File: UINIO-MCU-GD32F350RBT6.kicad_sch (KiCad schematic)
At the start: 33 parts, among them J1 Conn_01x32_Pin, J2 Conn_01x32_Pin, J3 Conn_01x04_Pin, SW1 BOOT0, SW2 NRST, U1 ME6211C33M5G-N, U2 GD32F350RBT6, Y1 32.768KHz, Y2 8MHz

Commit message: Release UINIO-MCU-GD32F350RBT6 version 3.2.0.
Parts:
- removed R4: 1M, Resistor_SMD:R_0603_1608Metric, symbol Device:R
- removed R9: 1.5K, Resistor_SMD:R_0603_1608Metric, symbol Device:R
- added C11: 0.1uF, Capacitor_SMD:C_0603_1608Metric, symbol Device:C
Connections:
- net GND: now also U2.12 (VSSA), C11.2; no longer L1.1
- net VBAT: now also C11.1
- net VDD_3.3V: now also L1.1; no longer U2.13 (VDDA)
- net VSSA: no longer names the net of L1.2
- net VSSA: now also U2.13 (VDDA); no longer U2.12 (VSSA)
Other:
- moved on the sheet: L1

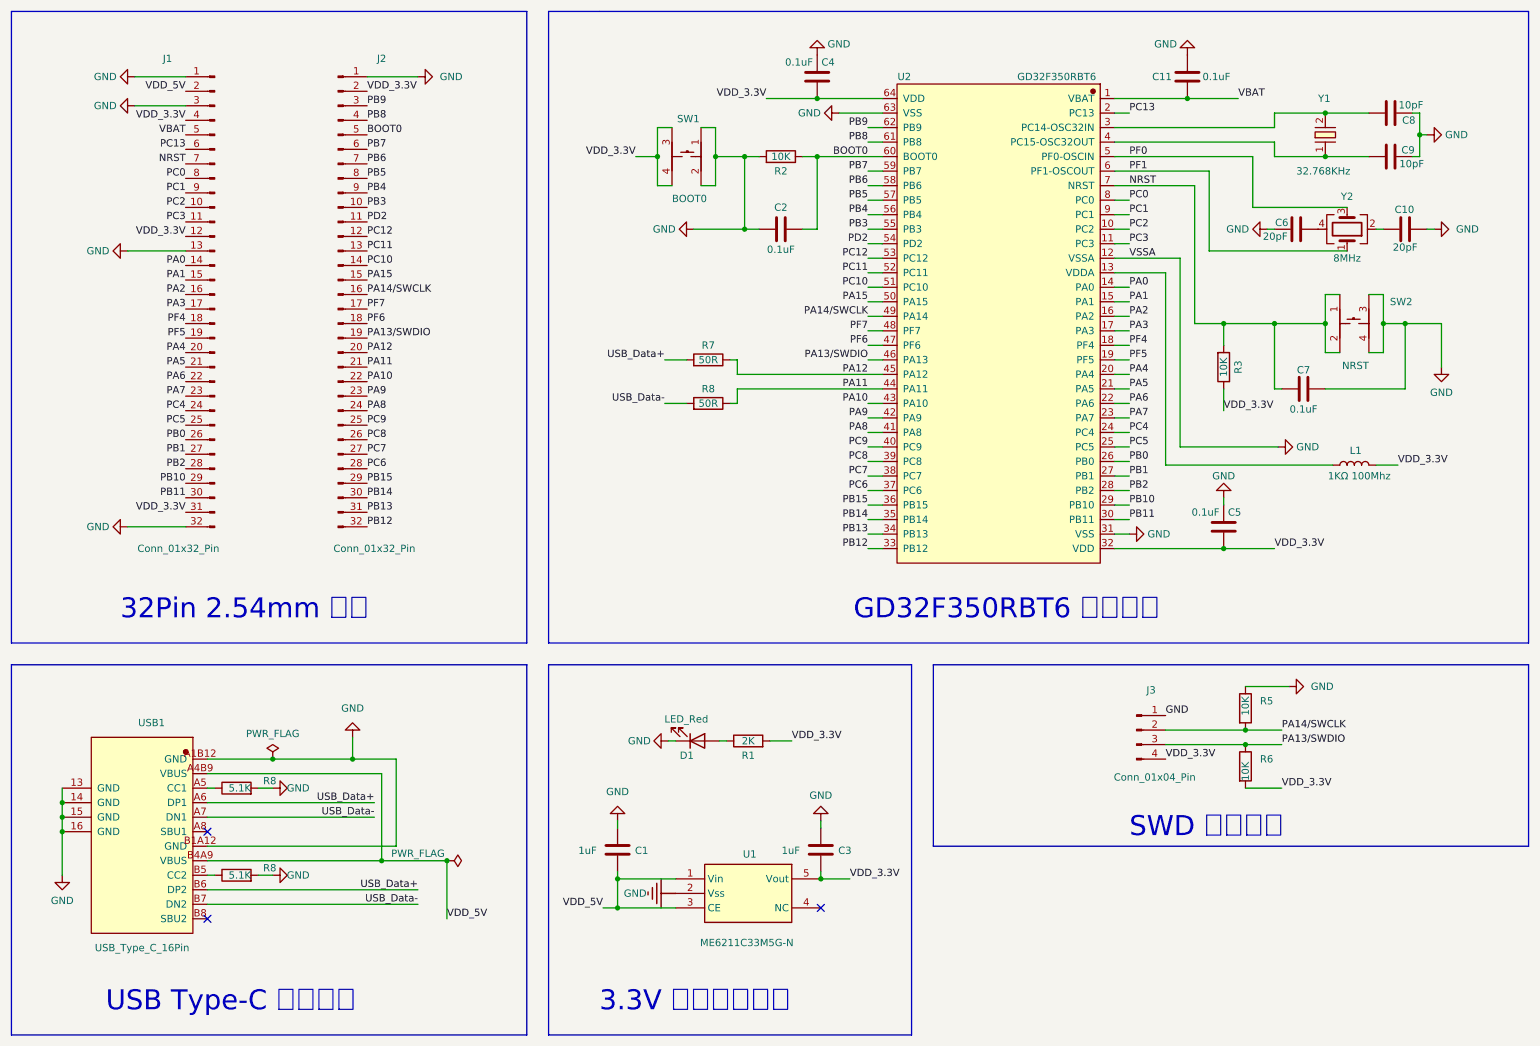
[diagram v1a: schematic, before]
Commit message: Release UINIO-MCU-GD32F350RBT6 version 3.3.0.
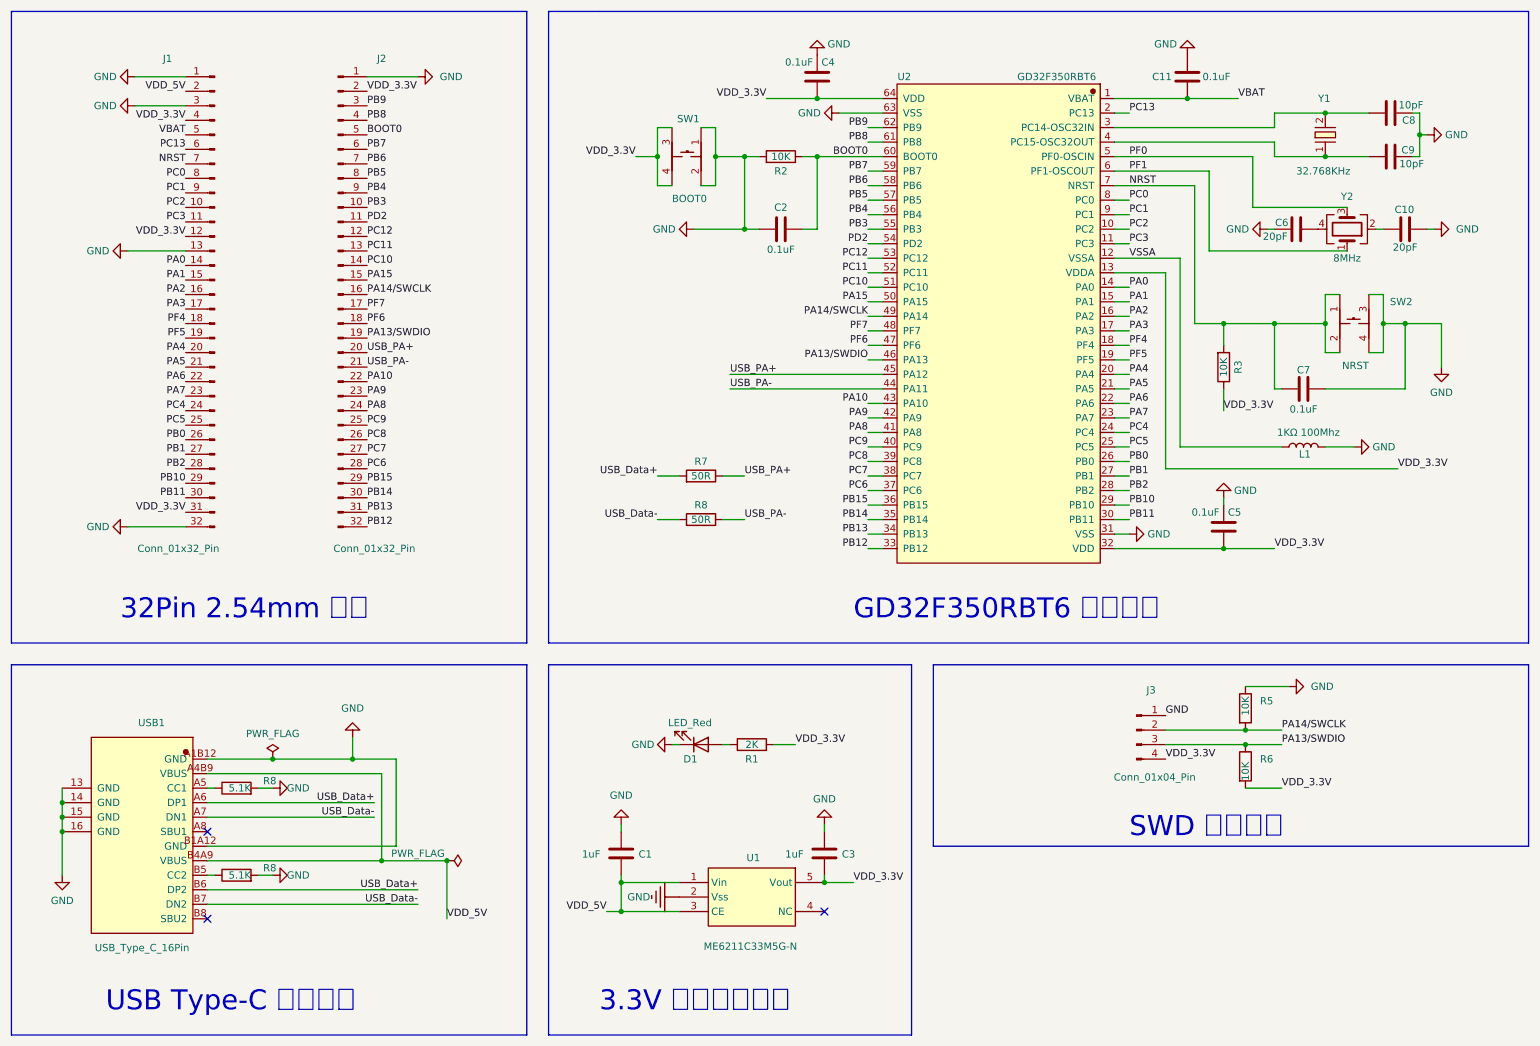
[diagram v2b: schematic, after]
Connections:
- net GND: now also L1.1; no longer U2.12 (VSSA)
- net VDD_3.3V: now also U2.13 (VDDA); no longer L1.1
- net VSSA: now reaches L1.2
- net VSSA: now also U2.12 (VSSA); no longer U2.13 (VDDA)
- net PA11 renamed USB_PA-
- net PA12 renamed USB_PA+
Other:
- moved on the sheet: C1, C3, D1, L1, R1, R7, R8, U1

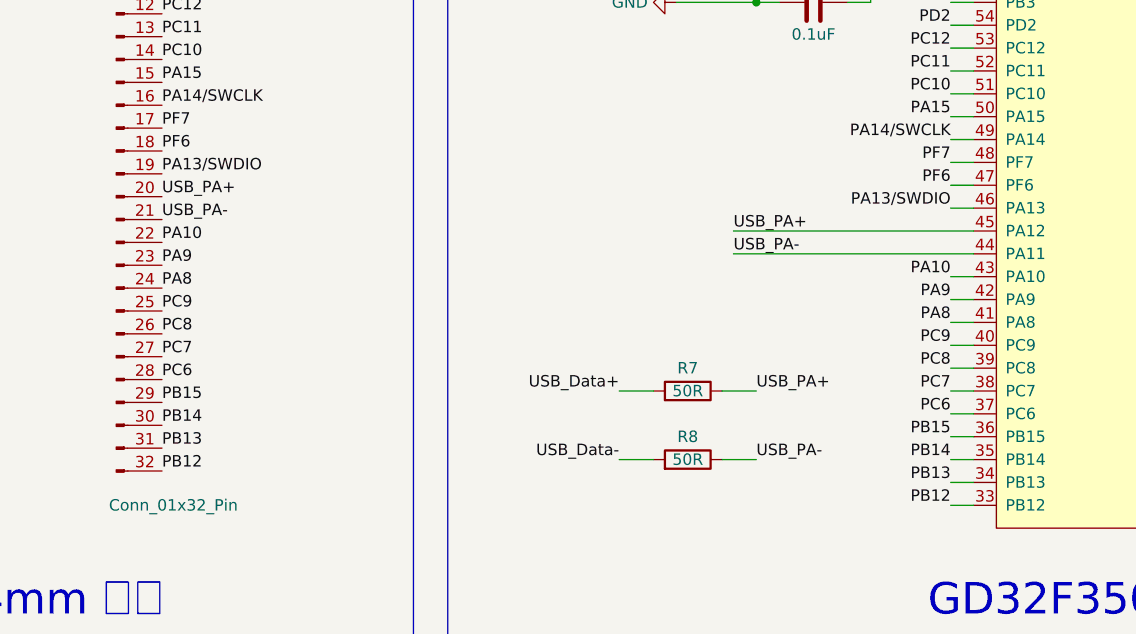
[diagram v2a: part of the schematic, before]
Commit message: Release UINIO-MCU-GD32F350RBT6 version 3.3.0.
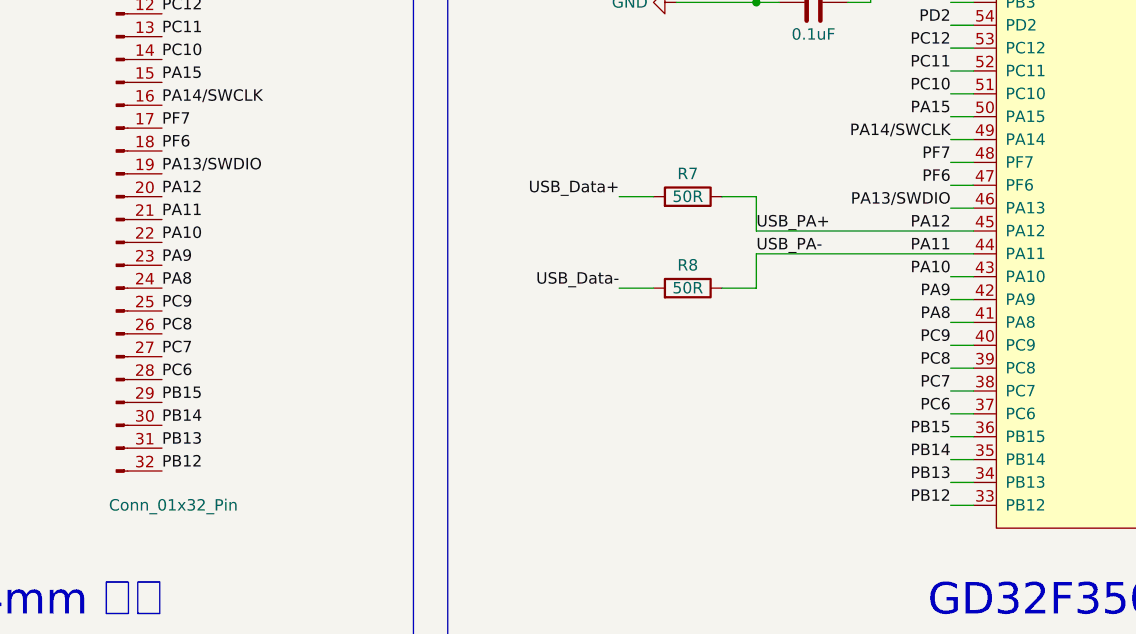
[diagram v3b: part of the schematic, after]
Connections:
- net USB_PA+ renamed PA12
- net USB_PA- renamed PA11
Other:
- moved on the sheet: R7, R8
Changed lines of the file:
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@@
+    (stroke (width 0) (type default))
+  )
+  (wire (pts (xy 144.78 82.55) (xy 168.91 82.55))
     (stroke (width 0) (type default))
   )
@@
     (stroke (width 0) (type default))
   )
-  (wire (pts (xy 129.54 105.41) (xy 133.35 105.41))
+  (wire (pts (xy 129.54 86.36) (xy 133.35 86.36))
     (stroke (width 0) (type default))
   )
@@
     (stroke (width 0) (type default))
   )
-  (wire (pts (xy 142.24 82.55) (xy 168.91 82.55))
+  (wire (pts (xy 140.97 86.36) (xy 144.78 86.36))
     (stroke (width 0) (type default))
   )
@@
   )
   (polyline (pts (xy 106.68 16.51) (xy 106.68 127))
-    (stroke (width 0) (type default))
-  )
-  (wire (pts (xy 140.97 105.41) (xy 144.78 105.41))
     (stroke (width 0) (type default))
   )
@@
     (stroke (width 0) (type default))
   )
+  (wire (pts (xy 144.78 86.36) (xy 144.78 82.55))
+    (stroke (width 0) (type default))
+  )
   (wire (pts (xy 166.37 36.83) (xy 168.91 36.83))
     (stroke (width 0) (type default))
@@
     (stroke (width 0) (type default))
   )
-  (wire (pts (xy 129.54 97.79) (xy 133.35 97.79))
+  (wire (pts (xy 129.54 76.2) (xy 133.35 76.2))
     (stroke (width 0) (type default))
   )
@@
     (stroke (width 0) (type default))
   )
+  (wire (pts (xy 144.78 80.01) (xy 168.91 80.01))
+    (stroke (width 0) (type default))
+  )
   (wire (pts (xy 166.37 72.39) (xy 168.91 72.39))
     (stroke (width 0) (type default))
@@
     (stroke (width 0) (type default))
   )
-  (wire (pts (xy 142.24 80.01) (xy 168.91 80.01))
+  (wire (pts (xy 140.97 76.2) (xy 144.78 76.2))
     (stroke (width 0) (type default))
   )
@@
     (stroke (width 0) (type default))
   )
+  (wire (pts (xy 144.78 76.2) (xy 144.78 80.01))
+    (stroke (width 0) (type default))
+  )
   (wire (pts (xy 166.37 44.45) (xy 168.91 44.45))
     (stroke (width 0) (type default))
@@
   )
   (polyline (pts (xy 281.94 162.56) (xy 177.8 162.56))
-    (stroke (width 0) (type default))
-  )
-  (wire (pts (xy 140.97 97.79) (xy 144.78 97.79))
     (stroke (width 0) (type default))
   )
@@
     (effects (font (size 1.27 1.27)) (justify right bottom))
   )
-  (label "USB_PA+" (at 144.78 97.79 0) (fields_autoplaced)
-    (effects (font (size 1.27 1.27)) (justify left bottom))
-  )
   (label "PB4" (at 166.37 52.07 180) (fields_autoplaced)
     (effects (font (size 1.27 1.27)) (justify right bottom))
@@
     (effects (font (size 1.27 1.27)) (justify right bottom))
   )
-  (label "USB_PA-" (at 144.78 105.41 0) (fields_autoplaced)
-    (effects (font (size 1.27 1.27)) (justify left bottom))
-  )
   (label "PB12" (at 78.74 106.68 0) (fields_autoplaced)
     (effects (font (size 1.27 1.27)) (justify left bottom))
@@
     (effects (font (size 1.27 1.27)) (justify left bottom))
   )
-  (label "USB_Data-" (at 129.54 105.41 180) (fields_autoplaced)
+  (label "USB_Data-" (at 129.54 86.36 180) (fields_autoplaced)
     (effects (font (size 1.27 1.27)) (justify right bottom))
   )
@@
     (effects (font (size 1.27 1.27)) (justify right bottom))
   )
-  (label "USB_Data+" (at 129.54 97.79 180) (fields_autoplaced)
+  (label "USB_Data+" (at 129.54 76.2 180) (fields_autoplaced)
     (effects (font (size 1.27 1.27)) (justify right bottom))
   )
@@
     (effects (font (size 1.27 1.27)) (justify right bottom))
   )
-  (label "USB_PA+" (at 78.74 76.2 0) (fields_autoplaced)
-    (effects (font (size 1.27 1.27)) (justify left bottom))
-  )
   (label "PB15" (at 166.37 102.87 180) (fields_autoplaced)
     (effects (font (size 1.27 1.27)) (justify right bottom))
@@
     (effects (font (size 1.27 1.27)) (justify right bottom))
   )
+  (label "PA12" (at 78.74 76.2 0) (fields_autoplaced)
+    (effects (font (size 1.27 1.27)) (justify left bottom))
+  )
   (label "PA1" (at 46.99 63.5 180) (fields_autoplaced)
     (effects (font (size 1.27 1.27)) (justify right bottom))
@@
     (effects (font (size 1.27 1.27)) (justify left bottom))
   )
+  (label "PA12" (at 166.37 80.01 180) (fields_autoplaced)
+    (effects (font (size 1.27 1.27)) (justify right bottom))
+  )
   (label "PB5" (at 166.37 49.53 180) (fields_autoplaced)
     (effects (font (size 1.27 1.27)) (justify right bottom))
   )
-  (label "USB_PA-" (at 78.74 78.74 0) (fields_autoplaced)
-    (effects (font (size 1.27 1.27)) (justify left bottom))
-  )
   (label "PC1" (at 46.99 48.26 180) (fields_autoplaced)
     (effects (font (size 1.27 1.27)) (justify right bottom))
@@
     (effects (font (size 1.27 1.27)) (justify left bottom))
   )
-  (label "USB_PA+" (at 142.24 80.01 0) (fields_autoplaced)
+  (label "USB_PA+" (at 144.78 80.01 0) (fields_autoplaced)
     (effects (font (size 1.27 1.27)) (justify left bottom))
   )
@@
     (effects (font (size 1.27 1.27)) (justify left bottom))
   )
+  (label "PA11" (at 166.37 82.55 180) (fields_autoplaced)
+    (effects (font (size 1.27 1.27)) (justify right bottom))
+  )
   (label "PC13" (at 46.99 40.64 180) (fields_autoplaced)
     (effects (font (size 1.27 1.27)) (justify right bottom))
   )
+  (label "PA11" (at 78.74 78.74 0) (fields_autoplaced)
+    (effects (font (size 1.27 1.27)) (justify left bottom))
+  )
   (label "PA7" (at 212.09 87.63 0) (fields_autoplaced)
     (effects (font (size 1.27 1.27)) (justify left bottom))
@@
     (effects (font (size 1.27 1.27)) (justify left bottom))
   )
-  (label "USB_PA-" (at 142.24 82.55 0) (fields_autoplaced)
+  (label "USB_PA-" (at 144.78 82.55 0) (fields_autoplaced)
     (effects (font (size 1.27 1.27)) (justify left bottom))
   )
@@
     )
   )
-  (symbol (lib_id "Device:R") (at 137.16 105.41 270) (mirror x) (unit 1)
-    (in_bom yes) (on_board yes) (dnp no)
-    (property "Reference" "R8" (at 137.16 102.87 90)
-      (effects (font (size 1.27 1.27)))
-    )
-    (property "Value" "50R" (at 137.16 105.41 90)
-      (effects (font (size 1.27 1.27)))
-    )
-    (property "Footprint" "Resistor_SMD:R_0603_1608Metric" (at 137.16 107.188 90)
-      (effects (font (size 1.27 1.27)) hide)
-    )
-    (property "Datasheet" "~" (at 137.16 105.41 0)
+  (symbol (lib_id "Device:R") (at 137.16 86.36 270) (mirror x) (unit 1)
+    (in_bom yes) (on_board yes) (dnp no)
+    (property "Reference" "R8" (at 137.16 83.82 90)
+      (effects (font (size 1.27 1.27)))
+    )
+    (property "Value" "50R" (at 137.16 86.36 90)
+      (effects (font (size 1.27 1.27)))
+    )
+    (property "Footprint" "Resistor_SMD:R_0603_1608Metric" (at 137.16 88.138 90)
+      (effects (font (size 1.27 1.27)) hide)
+    )
+    (property "Datasheet" "~" (at 137.16 86.36 0)
       (effects (font (size 1.27 1.27)) hide)
     )
@@
     )
   )
-  (symbol (lib_id "Device:R") (at 137.16 97.79 270) (mirror x) (unit 1)
-    (in_bom yes) (on_board yes) (dnp no)
-    (property "Reference" "R7" (at 137.16 95.25 90)
-      (effects (font (size 1.27 1.27)))
-    )
-    (property "Value" "50R" (at 137.16 97.79 90)
-      (effects (font (size 1.27 1.27)))
-    )
-    (property "Footprint" "Resistor_SMD:R_0603_1608Metric" (at 137.16 99.568 90)
-      (effects (font (size 1.27 1.27)) hide)
-    )
-    (property "Datasheet" "~" (at 137.16 97.79 0)
-      (effects (font (size 1.27 1.27)) hide)
-    )
+  (symbol (lib_id "Device:R") (at 137.16 76.2 270) (mirror x) (unit 1)
+    (in_bom yes) (on_board yes) (dnp no)
+    (property "Reference" "R7" (at 137.16 73.66 90)
+      (effects (font (size 1.27 1.27)))
+    )
+    (property "Value" "50R" (at 137.16 76.2 90)
+      (effects (font (size 1.27 1.27)))
+    )
+    (property "Footprint" "Resistor_SMD:R_0603_1608Metric" (at 137.16 77.978 90)
+      (effects (font (size 1.27 1.27)) hide)
+    )
+    (property "Datasheet" "~" (at 137.16 76.2 0)
+      (effects (font (size 1.27 1.27)) hide)
+    )
